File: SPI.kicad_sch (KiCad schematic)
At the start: 4 parts

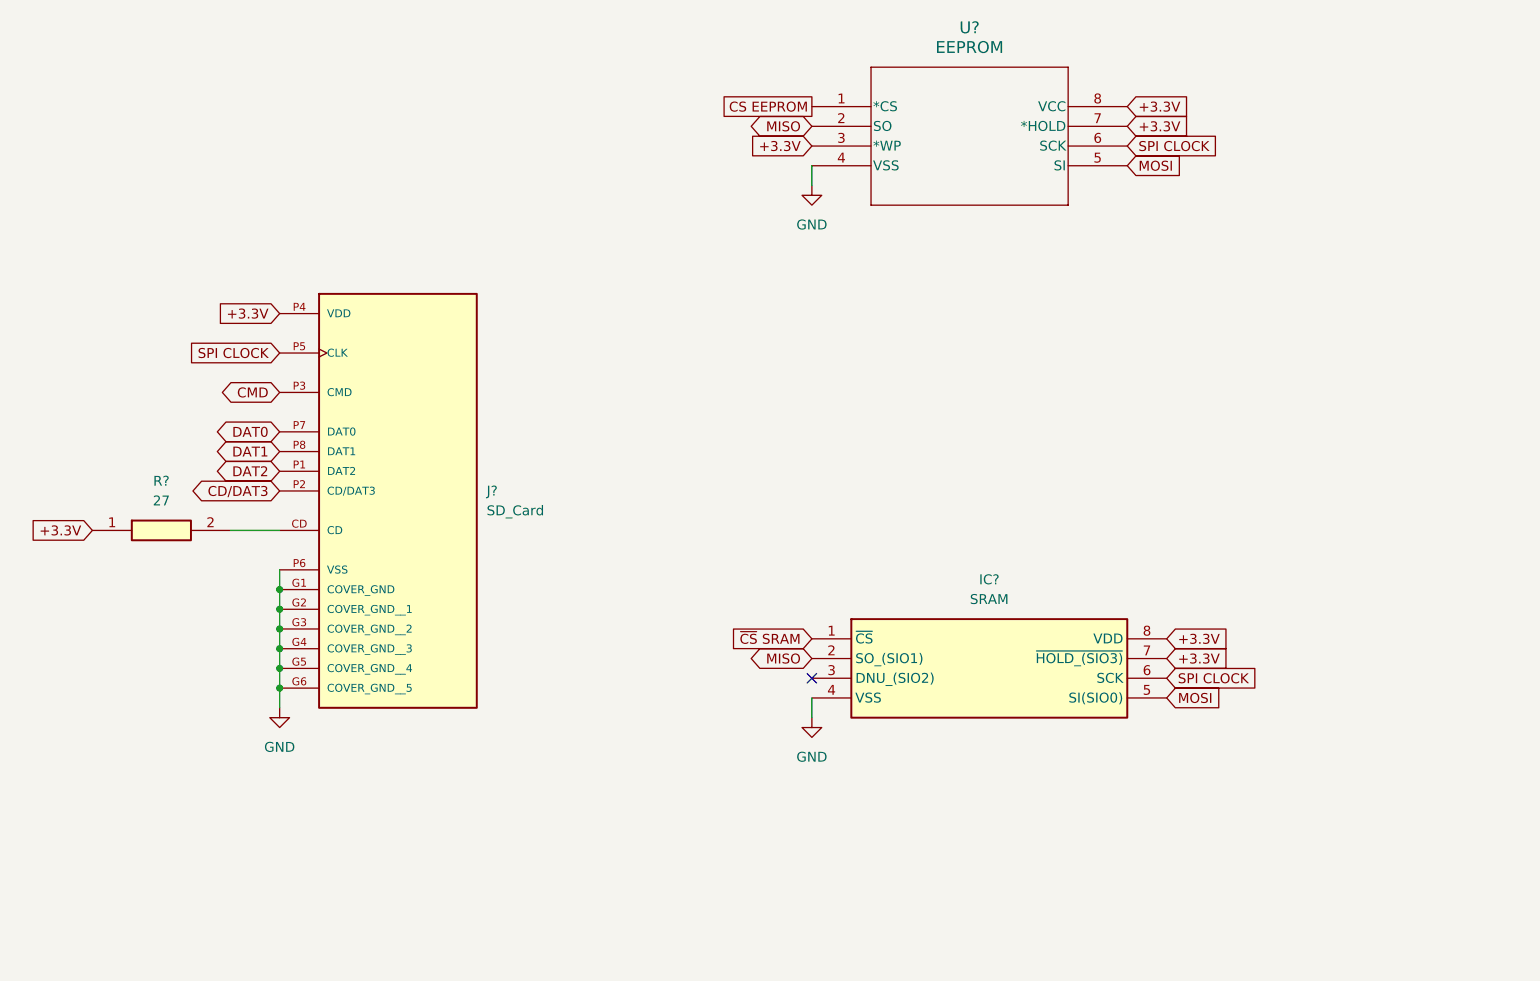
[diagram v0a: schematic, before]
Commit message: Updated SPI/Microcontroller
Updated SPI schematic and connected to microcontroller
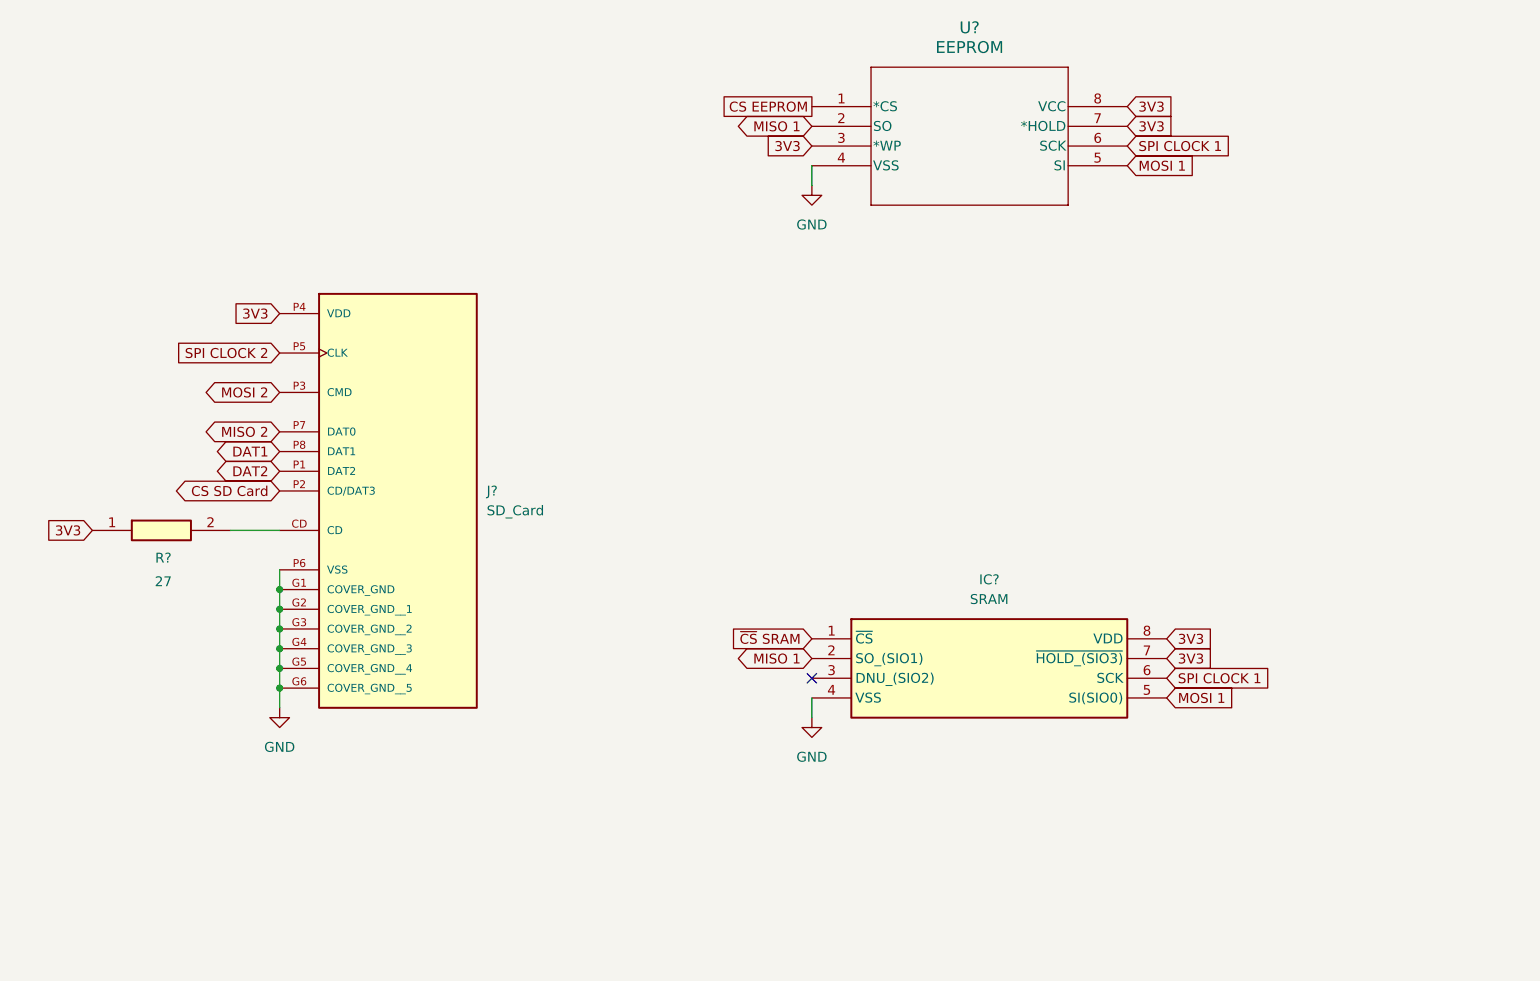
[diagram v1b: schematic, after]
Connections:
- net +3.3V renamed 3V3
- net CD/DAT3 renamed CS SD Card
- net CMD renamed MOSI 2
- net DAT0 renamed MISO 2
- net MISO renamed MISO 1
- net MOSI renamed MOSI 1
- net SPI CLOCK renamed SPI CLOCK 1
- net SPI CLOCK 1: no longer J?.P5 (CLK)
- new net SPI CLOCK 2: J?.P5 (CLK)
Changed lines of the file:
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@@
 		)
 	)
-	(global_label "+3.3V"
+	(global_label "3V3"
 		(shape input)
 		(at 163.83 49.53 0)
@@
 		)
 	)
-	(global_label "MISO"
+	(global_label "MISO 1"
 		(shape bidirectional)
 		(at 123.19 49.53 180)
@@
 		)
 	)
-	(global_label "SPI CLOCK"
+	(global_label "SPI CLOCK 1"
 		(shape input)
 		(at 163.83 52.07 0)
@@
 		)
 	)
-	(global_label "+3.3V"
+	(global_label "3V3"
 		(shape input)
 		(at 123.19 52.07 180)
@@
 		)
 	)
-	(global_label "CMD"
+	(global_label "MOSI 2"
 		(shape bidirectional)
 		(at 54.61 83.82 180)
@@
 		)
 	)
-	(global_label "+3.3V"
+	(global_label "3V3"
 		(shape input)
 		(at 168.91 115.57 0)
@@
 		)
 	)
-	(global_label "MOSI"
+	(global_label "MOSI 1"
 		(shape input)
 		(at 163.83 54.61 0)
@@
 		)
 	)
-	(global_label "+3.3V"
+	(global_label "3V3"
 		(shape input)
 		(at 54.61 73.66 180)
@@
 		)
 	)
-	(global_label "+3.3V"
+	(global_label "3V3"
 		(shape input)
 		(at 168.91 118.11 0)
@@
 		)
 	)
-	(global_label "+3.3V"
+	(global_label "3V3"
 		(shape input)
 		(at 30.48 101.6 180)
@@
 		)
 	)
-	(global_label "+3.3V"
+	(global_label "3V3"
 		(shape input)
 		(at 163.83 46.99 0)
@@
 		)
 	)
-	(global_label "MOSI"
+	(global_label "MOSI 1"
 		(shape input)
 		(at 168.91 123.19 0)
@@
 		)
 	)
-	(global_label "DAT0"
+	(global_label "MISO 2"
 		(shape bidirectional)
 		(at 54.61 88.9 180)
@@
 		)
 	)
-	(global_label "MISO"
+	(global_label "MISO 1"
 		(shape bidirectional)
 		(at 123.19 118.11 180)
@@
 		)
 	)
-	(global_label "SPI CLOCK"
+	(global_label "SPI CLOCK 2"
 		(shape input)
 		(at 54.61 78.74 180)
@@
 		)
 	)
-	(global_label "CD/DAT3"
+	(global_label "SPI CLOCK 1"
+		(shape input)
+		(at 168.91 120.65 0)
+		(effects
+			(font
+				(size 1.27 1.27)
+			)
+			(justify left)
+		)
+		(property "Intersheetrefs" "${INTERSHEET_REFS}"
+			(at 168.91 120.65 0)
+			(effects
+				(font
+					(size 1.27 1.27)
+				)
+				(hide yes)
+			)
+		)
+	)
+	(global_label "CS SD Card"
 		(shape bidirectional)
 		(at 54.61 96.52 180)
@@
 		(property "Intersheetrefs" "${INTERSHEET_REFS}"
 			(at 54.61 96.52 0)
-			(effects
-				(font
-					(size 1.27 1.27)
-				)
-				(hide yes)
-			)
-		)
-	)
-	(global_label "SPI CLOCK"
-		(shape input)
-		(at 168.91 120.65 0)
-		(effects
-			(font
-				(size 1.27 1.27)
-			)
-			(justify left)
-		)
-		(property "Intersheetrefs" "${INTERSHEET_REFS}"
-			(at 168.91 120.65 0)
 			(effects
 				(font
@@
 		(dnp no)
 		(fields_autoplaced yes)
-		(property "Reference" "#PWR02"
+		(property "Reference" "#PWR?"
 			(at 54.61 130.81 0)
 			(effects
@@
 		)
 		(instances
+			(project "harm_drone"
+				(path "/5ce3566e-4e0f-420e-9b0d-3952cd3c63fd/9ace3f70-8aef-468d-a7a3-d32e6ab166be"
+					(reference "#PWR?")
+					(unit 1)
+				)
+			)
 			(project "SPI"
 				(path "/a1dacf80-5959-4abc-a7b3-75daab69d2bc"
@@
 		(dnp no)
 		(fields_autoplaced yes)
-		(property "Reference" "#PWR03"
+		(property "Reference" "#PWR?"
 			(at 123.19 63.5 0)
 			(effects
@@
 		)
 		(instances
+			(project "harm_drone"
+				(path "/5ce3566e-4e0f-420e-9b0d-3952cd3c63fd/9ace3f70-8aef-468d-a7a3-d32e6ab166be"
+					(reference "#PWR?")
+					(unit 1)
+				)
+			)
 			(project "SPI"
 				(path "/a1dacf80-5959-4abc-a7b3-75daab69d2bc"
@@
 		(dnp no)
 		(fields_autoplaced yes)
-		(property "Reference" "#PWR01"
+		(property "Reference" "#PWR?"
 			(at 123.19 132.08 0)
 			(effects
@@
 		)
 		(instances
+			(project "harm_drone"
+				(path "/5ce3566e-4e0f-420e-9b0d-3952cd3c63fd/9ace3f70-8aef-468d-a7a3-d32e6ab166be"
+					(reference "#PWR?")
+					(unit 1)
+				)
+			)
 			(project ""
 				(path "/a1dacf80-5959-4abc-a7b3-75daab69d2bc"
@@
 		(on_board yes)
 		(dnp no)
-		(fields_autoplaced yes)
 		(property "Reference" "R?"
-			(at 39.37 95.25 0)
+			(at 39.624 105.156 0)
 			(effects
 				(font
@@
 		)
 		(property "Value" "27"
-			(at 39.37 97.79 0)
-			(effects
-				(font
+			(at 39.624 108.204 0)
+			(effects
+				(font

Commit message: finished up schematic
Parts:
- added J5: SPI2, symbol Connector:Conn_01x04_Pin
- added J6: SPI1, symbol Connector:Conn_01x05_Pin
- added R4, R5, R7, R8, R9: 10kOhm, Resistor_SMD:R_0805_2012Metric, symbol group127:Resistor
- IC3: renamed from IC?; footprint SOIC127P600X175-8N -> (none)
- J4: renamed from J?; footprint CUI_MSD-12-A -> (none)
- R6: renamed from R?; footprint RESC2012X60N -> Resistor_SMD:R_0805_2012Metric
- U2: renamed from U?; footprint SOIC8_ONS -> (none)
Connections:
- net 3V3: now also R4.1, R5.1, R7.1, R8.1, R9.1
- net CS EEPROM: now also J6.2 (Pin_2)
- net CS SD Card: now also J5.1 (Pin_1), R7.2
- net MISO 1: now also J6.4 (Pin_4)
- net MISO 2: now also J5.2 (Pin_2), R4.2
- net MOSI 1: now also J6.3 (Pin_3)
- net MOSI 2: now also J5.3 (Pin_3), R5.2
- net SPI CLOCK 1: now also J6.5 (Pin_5)
- net SPI CLOCK 2: now also J5.4 (Pin_4)
- net ~{CS} SRAM: now also J6.1 (Pin_1)
- net DAT1: no longer names the net of J4.P8 (DAT1)
- net DAT1: now also R9.2
- net DAT2: no longer names the net of J4.P1 (DAT2)
- net DAT2: now also R8.2
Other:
- moved on the sheet: J4, R6

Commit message: more footprint updates
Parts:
- J5: footprint (none) -> Connector_PinHeader_2.54mm:PinHeader_1x04_P2.54mm_Vertical
- J6: footprint (none) -> Connector_PinHeader_2.54mm:PinHeader_1x05_P2.54mm_Vertical
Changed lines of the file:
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@@
 			)
 		)
-		(property "Footprint" ""
+		(property "Footprint" "Connector_PinHeader_2.54mm:PinHeader_1x05_P2.54mm_Vertical"
 			(at 139.7 151.13 0)
 			(effects
@@
 			)
 		)
-		(property "Footprint" ""
+		(property "Footprint" "Connector_PinHeader_2.54mm:PinHeader_1x04_P2.54mm_Vertical"
 			(at 91.44 151.13 0)
 			(effects

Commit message: initial PCB draft!
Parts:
- added C23: 10uF, Capacitor_SMD:C_0805_2012Metric, symbol group127:0805Capacitor
- added C24: 0.1uF, Capacitor_SMD:C_0805_2012Metric, symbol group127:0805Capacitor
- IC3: footprint (none) -> group127:SRAM
- J4: footprint (none) -> group127:SDCard
- U2: footprint (none) -> group127:EEPROM
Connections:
- net 3V3: now also C23.2, C24.2
- net GND: now also C23.1, C24.1

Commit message: add PWM LED
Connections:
- net CARD_DETECT: now reaches J4.CD, R6.2
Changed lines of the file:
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@@
+	)
+	(junction
+		(at 64.77 101.6)
+		(diameter 0)
+		(color 0 0 0 0)
 	)
 	(junction
@@
 	(wire
 		(pts
-			(xy 60.96 101.6) (xy 67.31 101.6)
+			(xy 43.18 105.41) (xy 64.77 105.41)
+		)
+		(stroke
+			(width 0)
+			(type default)
+		)
+	)
+	(wire
+		(pts
+			(xy 60.96 101.6) (xy 64.77 101.6)
 		)
 		(stroke
@@
 	(wire
 		(pts
+			(xy 64.77 105.41) (xy 64.77 101.6)
+		)
+		(stroke
+			(width 0)
+			(type default)
+		)
+	)
+	(wire
+		(pts
 			(xy 119.38 153.67) (xy 134.62 153.67)
 		)
@@
 		(pts
 			(xy 59.69 60.96) (xy 59.69 91.44)
+		)
+		(stroke
+			(width 0)
+			(type default)
+		)
+	)
+	(wire
+		(pts
+			(xy 64.77 101.6) (xy 67.31 101.6)
 		)
 		(stroke
@@
 			(effects
 				(font
+					(size 1.27 1.27)
+				)
+				(hide yes)
+			)
+		)
+	)
+	(global_label "CARD_DETECT"
+		(shape input)
+		(at 43.18 105.41 180)
+		(effects
+			(font
+				(size 1.27 1.27)
+			)
+			(justify right)
+		)
+		(property "Intersheetrefs" "${INTERSHEET_REFS}"
+			(at 43.18 105.41 0)
+			(effects
+				(font

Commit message: schematic fixes are done
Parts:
- removed C23: 10uF, Capacitor_SMD:C_0805_2012Metric, symbol group127:0805Capacitor
- C24: value 0.1uF -> 2.2uF
- R6: value 27 -> 27ohm
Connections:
- net 3V3: now also C24.1; no longer C24.2
- net GND: now also C24.2; no longer C24.1
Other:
- moved on the sheet: C24
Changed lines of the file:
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@@
-	)
-	(junction
-		(at 77.47 69.85)
-		(diameter 0)
-		(color 0 0 0 0)
 	)
 	(junction
@@
 	)
 	(junction
+		(at 63.5 68.58)
+		(diameter 0)
+		(color 0 0 0 0)
+	)
+	(junction
 		(at 39.37 43.18)
 		(diameter 0)
@@
 		(color 0 0 0 0)
 	)
-	(junction
-		(at 83.82 57.15)
-		(diameter 0)
-		(color 0 0 0 0)
-	)
 	(no_connect
 		(at 123.19 120.65)
@@
 	(wire
 		(pts
+			(xy 63.5 67.31) (xy 63.5 68.58)
+		)
+		(stroke
+			(width 0)
+			(type default)
+		)
+	)
+	(wire
+		(pts
 			(xy 58.42 93.98) (xy 58.42 60.96)
 		)
@@
 	(wire
 		(pts
+			(xy 63.5 68.58) (xy 63.5 73.66)
+		)
+		(stroke
+			(width 0)
+			(type default)
+		)
+	)
+	(wire
+		(pts
 			(xy 67.31 121.92) (xy 67.31 124.46)
 		)
@@
 	(wire
 		(pts
-			(xy 77.47 69.85) (xy 90.17 69.85)
-		)
-		(stroke
-			(width 0)
-			(type default)
-		)
-	)
-	(wire
-		(pts
 			(xy 67.31 111.76) (xy 67.31 114.3)
 		)
@@
 	(wire
 		(pts
-			(xy 77.47 57.15) (xy 83.82 57.15)
-		)
-		(stroke
-			(width 0)
-			(type default)
-		)
-	)
-	(wire
-		(pts
 			(xy 53.34 71.12) (xy 53.34 83.82)
 		)
@@
 	(wire
 		(pts
-			(xy 63.5 69.85) (xy 77.47 69.85)
-		)
-		(stroke
-			(width 0)
-			(type default)
-		)
-	)
-	(wire
-		(pts
 			(xy 67.31 93.98) (xy 58.42 93.98)
 		)
@@
 	(wire
 		(pts
-			(xy 83.82 57.15) (xy 90.17 57.15)
-		)
-		(stroke
-			(width 0)
-			(type default)
-		)
-	)
-	(wire
-		(pts
 			(xy 46.99 96.52) (xy 49.53 96.52)
 		)
@@
 		(pts
 			(xy 67.31 119.38) (xy 67.31 121.92)
-		)
-		(stroke
-			(width 0)
-			(type default)
-		)
-	)
-	(wire
-		(pts
-			(xy 63.5 69.85) (xy 63.5 73.66)
 		)
 		(stroke
@@
 	(global_label "3V3"
 		(shape input)
-		(at 63.5 69.85 90)
+		(at 63.5 67.31 90)
 		(fields_autoplaced yes)
 		(effects
@@
 		)
 		(property "Intersheetrefs" "${INTERSHEET_REFS}"
-			(at 63.5 63.3572 90)
+			(at 63.5 60.8172 90)
 			(effects
 				(font
@@
 	(symbol
 		(lib_id "group127:0805Capacitor")
-		(at 90.17 57.15 270)
+		(at 63.5 68.58 0)
 		(unit 1)
 		(exclude_from_sim no)
@@
 		(fields_autoplaced yes)
 		(property "Reference" "C24"
-			(at 97.79 63.5 0)
-			(effects
-				(font
-					(size 1.27 1.27)
-				)
-			)
-		)
-		(property "Value" "0.1uF"
-			(at 95.25 63.5 0)
+			(at 69.85 60.96 0)
+			(effects
+				(font
+					(size 1.27 1.27)
+				)
+			)
+		)
+		(property "Value" "2.2uF"
+			(at 69.85 63.5 0)
 			(effects
 				(font
@@
 		)
 		(property "Footprint" "Capacitor_SMD:C_0805_2012Metric"
-			(at -6.02 66.04 0)
+			(at 72.39 164.77 0)
 			(effects
 				(font
@@
 		)
 		(property "Datasheet" "http://datasheets.avx.com/X7RDielectric.pdf"
-			(at -106.02 66.04 0)
+			(at 72.39 264.77 0)
 			(effects
 				(font
@@
 		)
 		(property "Description" "0805 X7R ceramic capacitor,100nF 50V AVX 0805 Standard 100nF Ceramic Multilayer Capacitor, 50 V dc, +125degC, X7R Dielectric,  /-10% SMD"
-			(at 90.17 57.15 0)
+			(at 63.5 68.58 0)
 			(effects
 				(font
@@
 		)
 		(property "Height" "0.94"
-			(at -306.02 66.04 0)
+			(at 72.39 464.77 0)
 			(effects
 				(font
@@
 		)
 		(property "Mouser Part Number" "581-08055C104K"
-			(at -406.02 66.04 0)
+			(at 72.39 564.77 0)
 			(effects
 				(font
@@
 		)
 		(property "Mouser Price/Stock" "https://www.mouser.co.uk/ProductDetail/KYOCERA-AVX/08055C104KAT2A?qs=2ujN4bDBNE9mJvapP%252BjopA%3D%3D"
-			(at -506.02 66.04 0)
+			(at 72.39 664.77 0)
 			(effects
 				(font
@@
 		)
 		(property "Manufacturer_Name" "Kyocera AVX"
-			(at -606.02 66.04 0)
+			(at 72.39 764.77 0)
 			(effects
 				(font
@@
 		)
 		(property "Manufacturer_Part_Number" "08055C104KAT2A"
-			(at -706.02 66.04 0)
+			(at 72.39 864.77 0)
 			(effects
 				(font
@@
 	(symbol
 		(lib_id "power:GND")
-		(at 83.82 57.15 0)
+		(at 76.2 68.58 0)
 		(unit 1)
 		(exclude_from_sim no)
@@
 		(on_board yes)
 		(dnp no)
-		(fields_autoplaced yes)
 		(property "Reference" "#PWR035"
-			(at 83.82 63.5 0)
+			(at 76.2 74.93 0)
 			(effects
 				(font
@@
 		)
 		(property "Value" "GND"
-			(at 83.82 62.23 0)
+			(at 80.518 68.326 0)
 			(effects
 				(font
@@
 		)
 		(property "Footprint" ""
-			(at 83.82 57.15 0)
+			(at 76.2 68.58 0)
 			(effects
 				(font
@@
 		)
 		(property "Datasheet" ""
-			(at 83.82 57.15 0)
+			(at 76.2 68.58 0)
 			(effects
 				(font
@@
 		)
 		(property "Description" "Power symbol creates a global label with name \"GND\" , ground"
-			(at 83.82 57.15 0)
+			(at 76.2 68.58 0)
 			(effects
 				(font
@@
 	)
 	(symbol
-		(lib_id "group127:0805Capacitor")
-		(at 77.47 57.15 270)
-		(unit 1)
-		(exclude_from_sim no)
-		(in_bom yes)
-		(on_board yes)
-		(dnp no)
-		(fields_autoplaced yes)
-		(property "Reference" "C23"
-			(at 85.09 63.5 0)
-			(effects
-				(font
-					(size 1.27 1.27)
-				)
-			)
-		)
-		(property "Value" "10uF"
-			(at 82.55 63.5 0)
-			(effects
-				(font
-					(size 1.27 1.27)
-				)
-			)
-		)
-		(property "Footprint" "Capacitor_SMD:C_0805_2012Metric"
-			(at -18.72 66.04 0)
-			(effects
-				(font
-					(size 1.27 1.27)
-				)
-				(justify left top)
-				(hide yes)
-			)
-		)
-		(property "Datasheet" "http://datasheets.avx.com/X7RDielectric.pdf"
-			(at -118.72 66.04 0)
-			(effects
-				(font
-					(size 1.27 1.27)
-				)
-				(justify left top)
-				(hide yes)
-			)
-		)
-		(property "Description" "0805 X7R ceramic capacitor,100nF 50V AVX 0805 Standard 100nF Ceramic Multilayer Capacitor, 50 V dc, +125degC, X7R Dielectric,  /-10% SMD"
-			(at 77.47 57.15 0)
-			(effects
-				(font
-					(size 1.27 1.27)
-				)
-				(hide yes)
-			)
-		)
-		(property "Height" "0.94"
-			(at -318.72 66.04 0)
-			(effects
-				(font
-					(size 1.27 1.27)
-				)
-				(justify left top)
-				(hide yes)
-			)
-		)
-		(property "Mouser Part Number" "581-08055C104K"
-			(at -418.72 66.04 0)
-			(effects
-				(font
-					(size 1.27 1.27)
-				)
-				(justify left top)
-				(hide yes)
-			)
-		)
-		(property "Mouser Price/Stock" "https://www.mouser.co.uk/ProductDetail/KYOCERA-AVX/08055C104KAT2A?qs=2ujN4bDBNE9mJvapP%252BjopA%3D%3D"
-			(at -518.72 66.04 0)
-			(effects
-				(font
-					(size 1.27 1.27)
-				)
-				(justify left top)
-				(hide yes)
-			)
-		)
-		(property "Manufacturer_Name" "Kyocera AVX"
-			(at -618.72 66.04 0)
-			(effects
-				(font
-					(size 1.27 1.27)
-				)
-				(justify left top)
-				(hide yes)
-			)
-		)
-		(property "Manufacturer_Part_Number" "08055C104KAT2A"
-			(at -718.72 66.04 0)
-			(effects
-				(font
-					(size 1.27 1.27)
-				)
-				(justify left top)
-				(hide yes)
-			)
-		)
-		(pin "1"
-		)
-		(pin "2"
-		)
-		(instances
-			(project "harm_drone"
-				(path "/5ce3566e-4e0f-420e-9b0d-3952cd3c63fd/9ace3f70-8aef-468d-a7a3-d32e6ab166be"
-					(reference "C23")
-					(unit 1)
-				)
-			)
-		)
-	)
-	(symbol
 		(lib_id "group127:MSD-12-A")
 		(at 82.55 91.44 0)
@@
 			)
 		)
-		(property "Value" "27"
+		(property "Value" "27ohm"
 			(at 52.324 108.204 0)
 			(effects

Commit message: final changes
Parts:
- added C25, C26: 2.2uF, Capacitor_SMD:C_0805_2012Metric, symbol group127:0805Capacitor
- renumbered IC3 to IC4, J4 to J5, J5 to J6, J6 to J7, R4 to R19, R5 to R20, R6 to R21, R7 to R22, R8 to R23, R9 to R24
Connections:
- net 3V3: now also C25.1, C26.1
- net GND: now also C25.2, C26.2
